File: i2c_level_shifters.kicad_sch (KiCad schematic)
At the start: 3 parts, among them U25 NTS0104_DHVQFN

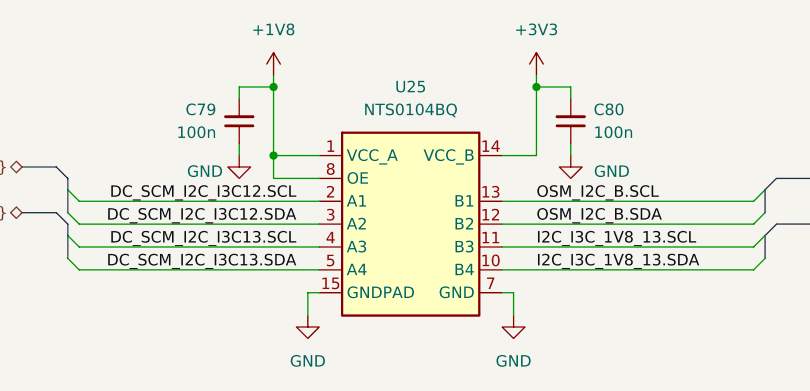
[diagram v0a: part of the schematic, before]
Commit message: [#83148] Connect the level shifters, change STBY bus to individual signals
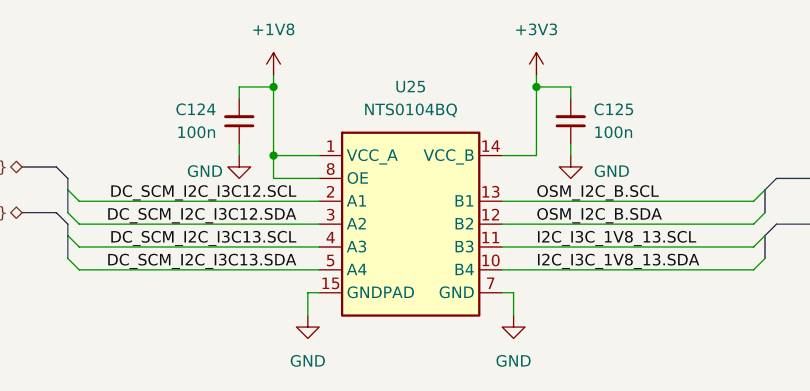
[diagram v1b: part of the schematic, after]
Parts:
- renumbered C79 to C124, C80 to C125
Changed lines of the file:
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@@
 		(instances
 			(project "bmc-reference-carrier-board"
-				(path "/5f636c45-3c15-4731-8931-4625e0dab7e4/18e2176b-772e-4e94-b8bf-eb9d5f80adf9"
+				(path "/5f636c45-3c15-4731-8931-4625e0dab7e4/1ae89ab2-a757-4731-85b8-826e038b4e67"
 					(reference "U25")
 					(unit 1)
@@
 		(on_board yes)
 		(dnp no)
-		(property "Reference" "C79"
+		(property "Reference" "C124"
 			(at 128.27 88.8936 90)
 			(effects
@@
 		(instances
 			(project "bmc-reference-carrier-board"
-				(path "/5f636c45-3c15-4731-8931-4625e0dab7e4/18e2176b-772e-4e94-b8bf-eb9d5f80adf9"
-					(reference "C79")
+				(path "/5f636c45-3c15-4731-8931-4625e0dab7e4/1ae89ab2-a757-4731-85b8-826e038b4e67"
+					(reference "C124")
 					(unit 1)
 				)
@@
 		(dnp no)
 		(fields_autoplaced yes)
-		(property "Reference" "#PWR0143"
+		(property "Reference" "#PWR0148"
 			(at 179.07 85.09 0)
 			(effects
@@
 		(instances
 			(project "bmc-reference-carrier-board"
-				(path "/5f636c45-3c15-4731-8931-4625e0dab7e4/18e2176b-772e-4e94-b8bf-eb9d5f80adf9"
-					(reference "#PWR0143")
+				(path "/5f636c45-3c15-4731-8931-4625e0dab7e4/1ae89ab2-a757-4731-85b8-826e038b4e67"
+					(reference "#PWR0148")
 					(unit 1)
 				)
@@
 		(dnp no)
 		(fields_autoplaced yes)
-		(property "Reference" "#PWR0142"
+		(property "Reference" "#PWR0152"
 			(at 152.4 114.3 0)
 			(effects
@@
 		(instances
 			(project "bmc-reference-carrier-board"
-				(path "/5f636c45-3c15-4731-8931-4625e0dab7e4/18e2176b-772e-4e94-b8bf-eb9d5f80adf9"
-					(reference "#PWR0142")
+				(path "/5f636c45-3c15-4731-8931-4625e0dab7e4/1ae89ab2-a757-4731-85b8-826e038b4e67"
+					(reference "#PWR0152")
 					(unit 1)
 				)
@@
 		(on_board yes)
 		(dnp no)
-		(property "Reference" "#PWR0139"
+		(property "Reference" "#PWR0149"
 			(at 121.92 96.52 0)
 			(effects
@@
 		(instances
 			(project "bmc-reference-carrier-board"
-				(path "/5f636c45-3c15-4731-8931-4625e0dab7e4/18e2176b-772e-4e94-b8bf-eb9d5f80adf9"
-					(reference "#PWR0139")
+				(path "/5f636c45-3c15-4731-8931-4625e0dab7e4/1ae89ab2-a757-4731-85b8-826e038b4e67"
+					(reference "#PWR0149")
 					(unit 1)
 				)
@@
 		(dnp no)
 		(fields_autoplaced yes)
-		(property "Reference" "#PWR0141"
+		(property "Reference" "#PWR0151"
 			(at 129.54 114.3 0)
 			(effects
@@
 		(instances
 			(project "bmc-reference-carrier-board"
-				(path "/5f636c45-3c15-4731-8931-4625e0dab7e4/18e2176b-772e-4e94-b8bf-eb9d5f80adf9"
-					(reference "#PWR0141")
+				(path "/5f636c45-3c15-4731-8931-4625e0dab7e4/1ae89ab2-a757-4731-85b8-826e038b4e67"
+					(reference "#PWR0151")
 					(unit 1)
 				)
@@
 		(dnp no)
 		(fields_autoplaced yes)
-		(property "Reference" "C80"
+		(property "Reference" "C125"
 			(at 170.18 88.8936 90)
 			(effects
@@
 		(instances
 			(project "bmc-reference-carrier-board"
-				(path "/5f636c45-3c15-4731-8931-4625e0dab7e4/18e2176b-772e-4e94-b8bf-eb9d5f80adf9"
-					(reference "C80")
+				(path "/5f636c45-3c15-4731-8931-4625e0dab7e4/1ae89ab2-a757-4731-85b8-826e038b4e67"
+					(reference "C125")
 					(unit 1)
 				)
@@
 		(dnp no)
 		(fields_autoplaced yes)
-		(property "Reference" "#PWR0140"
+		(property "Reference" "#PWR0147"
 			(at 149.86 87.63 0)
 			(effects
@@
 		(instances
 			(project "bmc-reference-carrier-board"
-				(path "/5f636c45-3c15-4731-8931-4625e0dab7e4/18e2176b-772e-4e94-b8bf-eb9d5f80adf9"
-					(reference "#PWR0140")
+				(path "/5f636c45-3c15-4731-8931-4625e0dab7e4/1ae89ab2-a757-4731-85b8-826e038b4e67"
+					(reference "#PWR0147")
 					(unit 1)
 				)
@@
 		(on_board yes)
 		(dnp no)
-		(property "Reference" "#PWR0146"
+		(property "Reference" "#PWR0150"
 			(at 176.53 96.52 0)
 			(effects
@@
 		(instances
 			(project "bmc-reference-carrier-board"
-				(path "/5f636c45-3c15-4731-8931-4625e0dab7e4/18e2176b-772e-4e94-b8bf-eb9d5f80adf9"
-					(reference "#PWR0146")
+				(path "/5f636c45-3c15-4731-8931-4625e0dab7e4/1ae89ab2-a757-4731-85b8-826e038b4e67"
+					(reference "#PWR0150")
 					(unit 1)
 				)

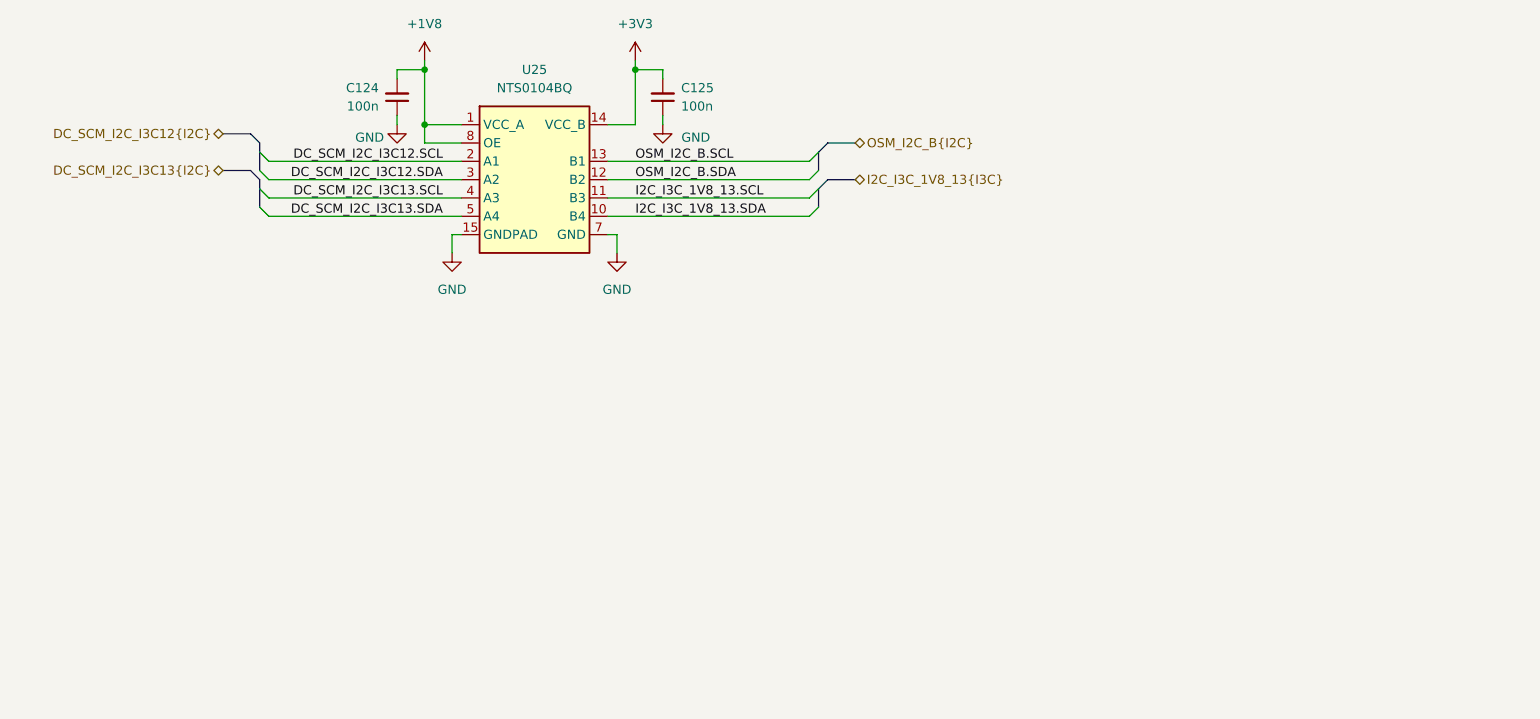
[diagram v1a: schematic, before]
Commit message: Changed A4 sheets to A3 and cleaned them up
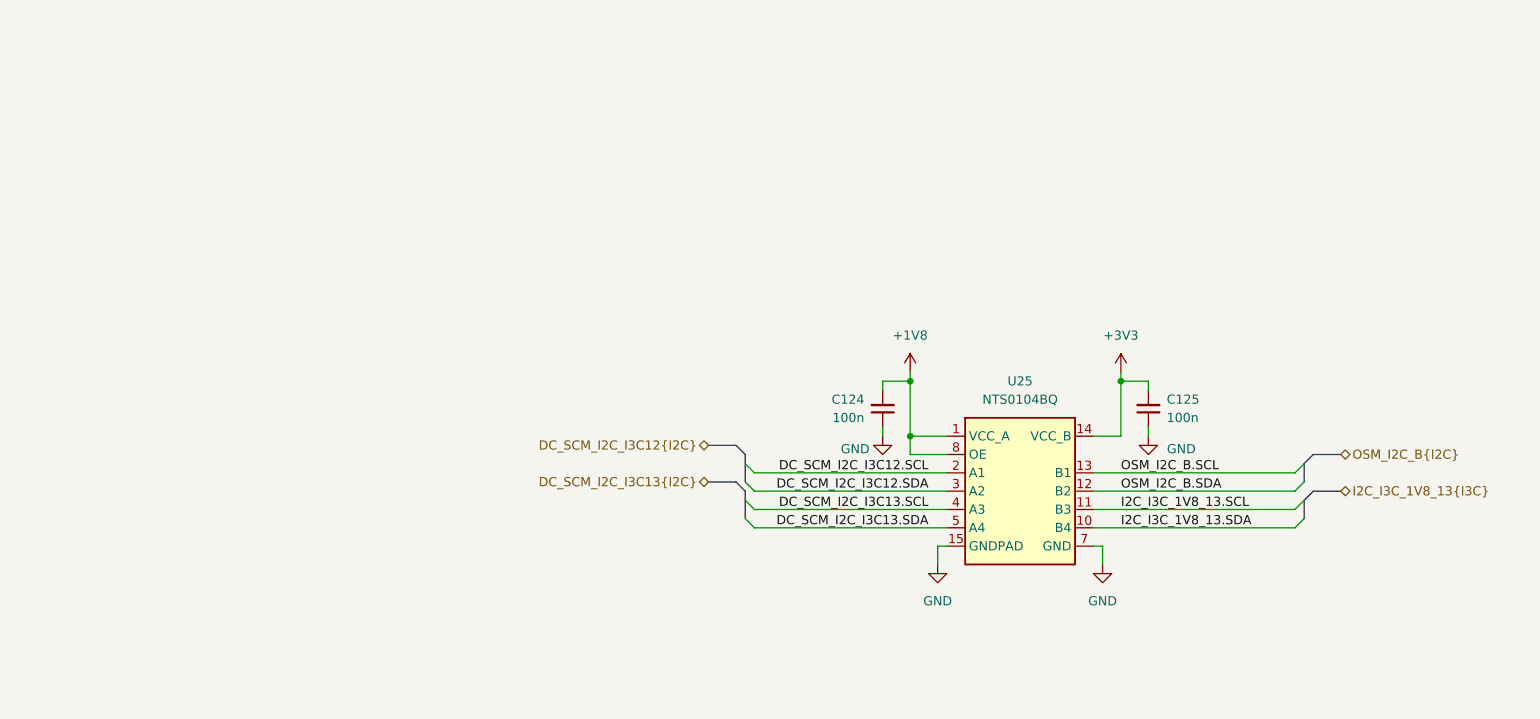
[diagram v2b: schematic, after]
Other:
- title: (none) -> BMC Reference Carrier Board
- moved on the sheet: C124, C125, U25

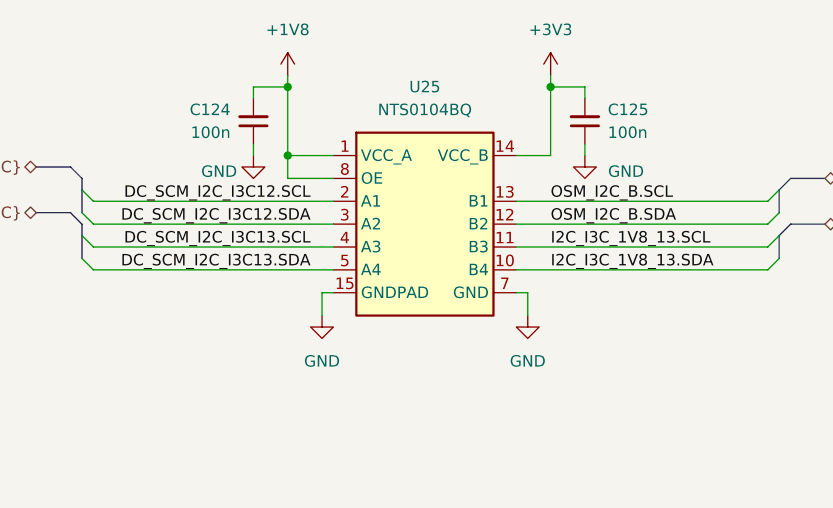
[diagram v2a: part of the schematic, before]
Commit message: Added level shifter bypass
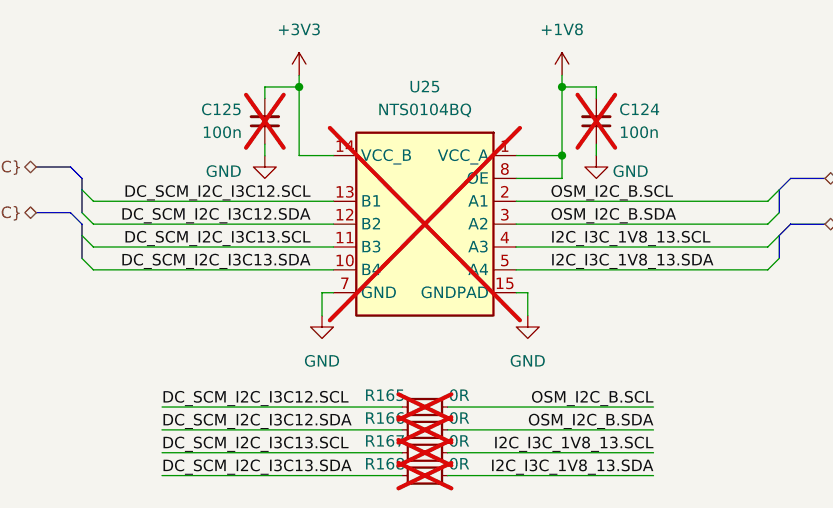
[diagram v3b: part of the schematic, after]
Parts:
- added R165, R166, R167, R168: R_0R_0402, antmicro-footprints:R_0402_1005Metric, symbol antmicroResistors0402:R_0R_0402
- C124, C125, U25: now not fitted
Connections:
- net DC_SCM_I2C_I3C12.SCL: now also U25.13 (B1), R165.1; no longer U25.2 (A1)
- net DC_SCM_I2C_I3C12.SDA: now also U25.12 (B2), R166.1; no longer U25.3 (A2)
- net DC_SCM_I2C_I3C13.SCL: now also U25.11 (B3), R167.1; no longer U25.4 (A3)
- net DC_SCM_I2C_I3C13.SDA: now also U25.10 (B4), R168.1; no longer U25.5 (A4)
- net I2C_I3C_1V8_13.SCL: now also U25.4 (A3), R167.2; no longer U25.11 (B3)
- net I2C_I3C_1V8_13.SDA: now also U25.5 (A4), R168.2; no longer U25.10 (B4)
- net OSM_I2C_B.SCL: now also U25.2 (A1), R165.2; no longer U25.13 (B1)
- net OSM_I2C_B.SDA: now also U25.3 (A2), R166.2; no longer U25.12 (B2)

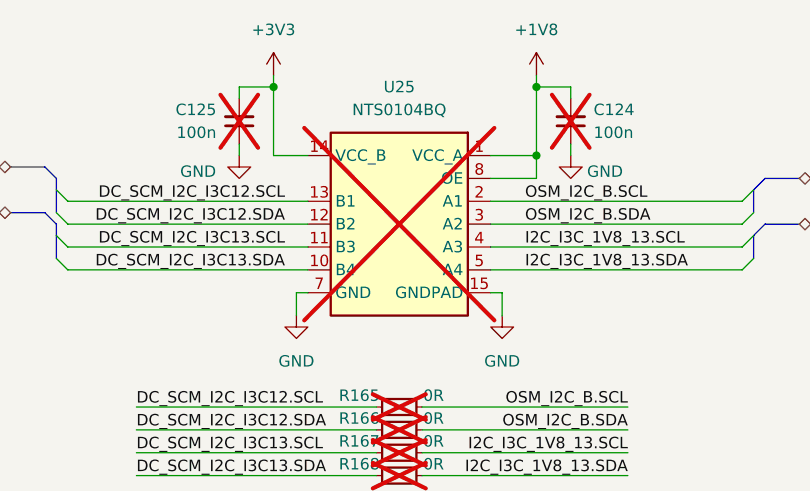
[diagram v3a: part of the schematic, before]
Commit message: [#83362] Fix connections of headers, add I2C mux
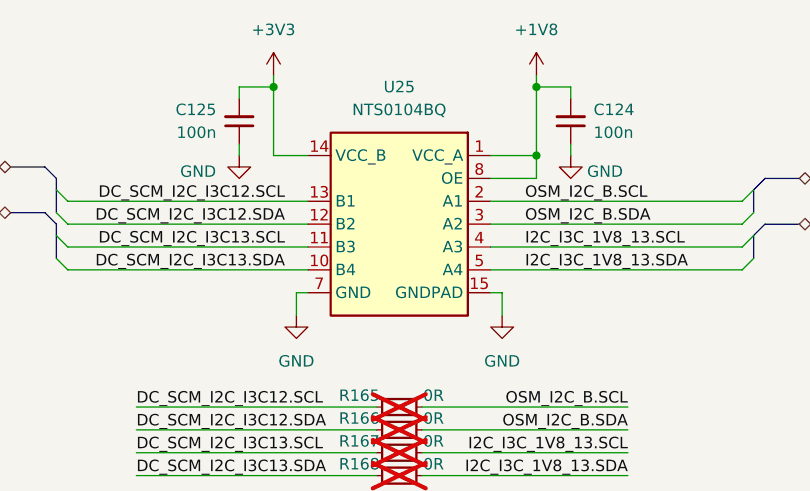
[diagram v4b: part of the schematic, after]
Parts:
- C124, C125, U25: now fitted
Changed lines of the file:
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@@
 		(in_bom yes)
 		(on_board yes)
-		(dnp yes)
+		(dnp no)
 		(fields_autoplaced yes)
 		(property "Reference" "U25"
@@
 		(in_bom yes)
 		(on_board yes)
-		(dnp yes)
+		(dnp no)
 		(property "Reference" "C124"
 			(at 238.76 132.0736 90)
@@
 		(in_bom yes)
 		(on_board yes)
-		(dnp yes)
+		(dnp no)
 		(fields_autoplaced yes)
 		(property "Reference" "C125"

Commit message: [#83609] Reannotate board
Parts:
- renumbered C125 to C162, C124 to C163, R165 to R283, R166 to R284, R167 to R285, R168 to R286, U25 to U33
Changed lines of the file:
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@@
 		(dnp no)
 		(fields_autoplaced yes)
-		(property "Reference" "U25"
+		(property "Reference" "U33"
 			(at 217.17 129.54 0)
 			(effects
@@
 			(project "bmc-reference-carrier-board"
 				(path "/5f636c45-3c15-4731-8931-4625e0dab7e4/1ae89ab2-a757-4731-85b8-826e038b4e67"
-					(reference "U25")
+					(reference "U33")
 					(unit 1)
 				)
@@
 		(on_board yes)
 		(dnp no)
-		(property "Reference" "C124"
+		(property "Reference" "C163"
 			(at 238.76 132.0736 90)
 			(effects
@@
 			(project "bmc-reference-carrier-board"
 				(path "/5f636c45-3c15-4731-8931-4625e0dab7e4/1ae89ab2-a757-4731-85b8-826e038b4e67"
-					(reference "C124")
+					(reference "C163")
 					(unit 1)
 				)
@@
 		(dnp no)
 		(fields_autoplaced yes)
-		(property "Reference" "#PWR0148"
+		(property "Reference" "#PWR0314"
 			(at 187.96 128.27 0)
 			(effects
@@
 			(project "bmc-reference-carrier-board"
 				(path "/5f636c45-3c15-4731-8931-4625e0dab7e4/1ae89ab2-a757-4731-85b8-826e038b4e67"
-					(reference "#PWR0148")
+					(reference "#PWR0314")
 					(unit 1)
 				)
@@
 		(on_board yes)
 		(dnp yes)
-		(property "Reference" "R166"
+		(property "Reference" "R284"
 			(at 212.725 166.37 0)
 			(effects
@@
 			(project "bmc-reference-carrier-board"
 				(path "/5f636c45-3c15-4731-8931-4625e0dab7e4/1ae89ab2-a757-4731-85b8-826e038b4e67"
-					(reference "R166")
+					(reference "R284")
 					(unit 1)
 				)
@@
 		(dnp no)
 		(fields_autoplaced yes)
-		(property "Reference" "#PWR0152"
+		(property "Reference" "#PWR0315"
 			(at 214.63 157.48 0)
 			(effects
@@
 			(project "bmc-reference-carrier-board"
 				(path "/5f636c45-3c15-4731-8931-4625e0dab7e4/1ae89ab2-a757-4731-85b8-826e038b4e67"
-					(reference "#PWR0152")
+					(reference "#PWR0315")
 					(unit 1)
 				)
@@
 		(on_board yes)
 		(dnp yes)
-		(property "Reference" "R167"
+		(property "Reference" "R285"
 			(at 212.725 168.91 0)
 			(effects
@@
 			(project "bmc-reference-carrier-board"
 				(path "/5f636c45-3c15-4731-8931-4625e0dab7e4/1ae89ab2-a757-4731-85b8-826e038b4e67"
-					(reference "R167")
+					(reference "R285")
 					(unit 1)
 				)
@@
 		(on_board yes)
 		(dnp no)
-		(property "Reference" "#PWR0149"
+		(property "Reference" "#PWR0318"
 			(at 245.11 139.7 0)
 			(effects
@@
 			(project "bmc-reference-carrier-board"
 				(path "/5f636c45-3c15-4731-8931-4625e0dab7e4/1ae89ab2-a757-4731-85b8-826e038b4e67"
-					(reference "#PWR0149")
+					(reference "#PWR0318")
 					(unit 1)
 				)
@@
 		(dnp no)
 		(fields_autoplaced yes)
-		(property "Reference" "#PWR0151"
+		(property "Reference" "#PWR0316"
 			(at 237.49 157.48 0)
 			(effects
@@
 			(project "bmc-reference-carrier-board"
 				(path "/5f636c45-3c15-4731-8931-4625e0dab7e4/1ae89ab2-a757-4731-85b8-826e038b4e67"
-					(reference "#PWR0151")
+					(reference "#PWR0316")
 					(unit 1)
 				)
@@
 		(dnp no)
 		(fields_autoplaced yes)
-		(property "Reference" "C125"
+		(property "Reference" "C162"
 			(at 196.85 132.0736 90)
 			(effects
@@
 			(project "bmc-reference-carrier-board"
 				(path "/5f636c45-3c15-4731-8931-4625e0dab7e4/1ae89ab2-a757-4731-85b8-826e038b4e67"
-					(reference "C125")
+					(reference "C162")
 					(unit 1)
 				)
@@
 		(dnp no)
 		(fields_autoplaced yes)
-		(property "Reference" "#PWR0147"
+		(property "Reference" "#PWR0317"
 			(at 217.17 130.81 0)
 			(effects
@@
 			(project "bmc-reference-carrier-board"
 				(path "/5f636c45-3c15-4731-8931-4625e0dab7e4/1ae89ab2-a757-4731-85b8-826e038b4e67"
-					(reference "#PWR0147")
+					(reference "#PWR0317")
 					(unit 1)
 				)
@@
 		(on_board yes)
 		(dnp yes)
-		(property "Reference" "R165"
+		(property "Reference" "R283"
 			(at 212.725 163.83 0)
 			(effects
@@
 			(project ""
 				(path "/5f636c45-3c15-4731-8931-4625e0dab7e4/1ae89ab2-a757-4731-85b8-826e038b4e67"
-					(reference "R165")
+					(reference "R283")
 					(unit 1)
 				)
@@
 		(on_board yes)
 		(dnp yes)
-		(property "Reference" "R168"
+		(property "Reference" "R286"
 			(at 212.725 171.45 0)
 			(effects
@@
 			(project "bmc-reference-carrier-board"
 				(path "/5f636c45-3c15-4731-8931-4625e0dab7e4/1ae89ab2-a757-4731-85b8-826e038b4e67"
-					(reference "R168")
+					(reference "R286")
 					(unit 1)
 				)
@@
 		(on_board yes)
 		(dnp no)
-		(property "Reference" "#PWR0150"
+		(property "Reference" "#PWR0313"
 			(at 190.5 139.7 0)
 			(effects
@@
 			(project "bmc-reference-carrier-board"
 				(path "/5f636c45-3c15-4731-8931-4625e0dab7e4/1ae89ab2-a757-4731-85b8-826e038b4e67"
-					(reference "#PWR0150")
+					(reference "#PWR0313")
 					(unit 1)
 				)
